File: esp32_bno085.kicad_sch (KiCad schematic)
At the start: 36 parts, among them J1 530480210, J2 USB_C_Receptacle_USB2.0_16P, Q1 AO3401A, SW1 RESET, SW2 BOOT, U1 TP4056-42-ESOP8, U2 ESP32-S3-WROOM-1, U3 BNO085, U4 XC6220B331MR, Y1 32.7680kHz

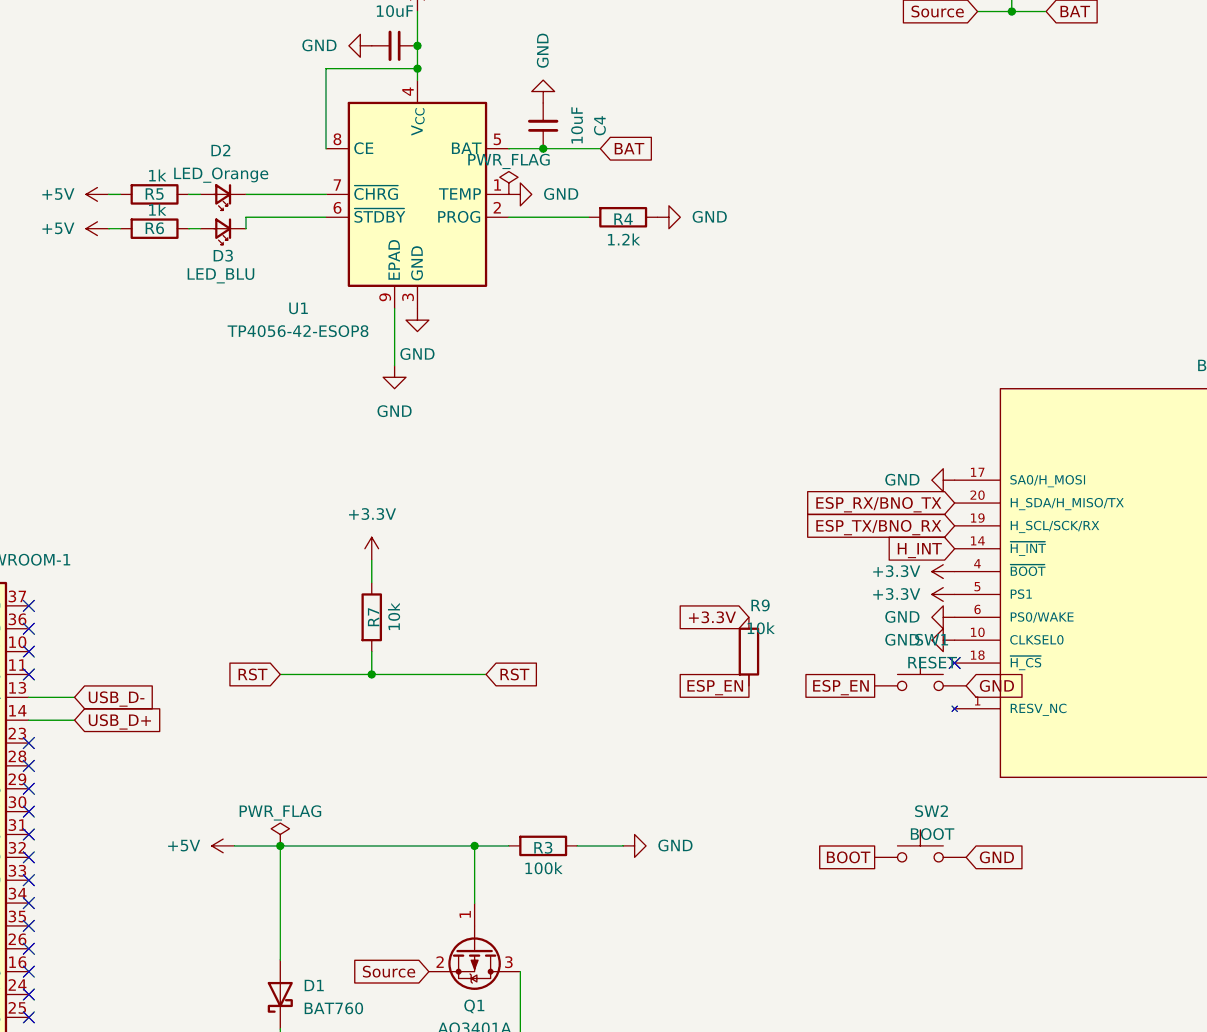
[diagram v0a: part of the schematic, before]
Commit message: Clean KiCad DRC warnings
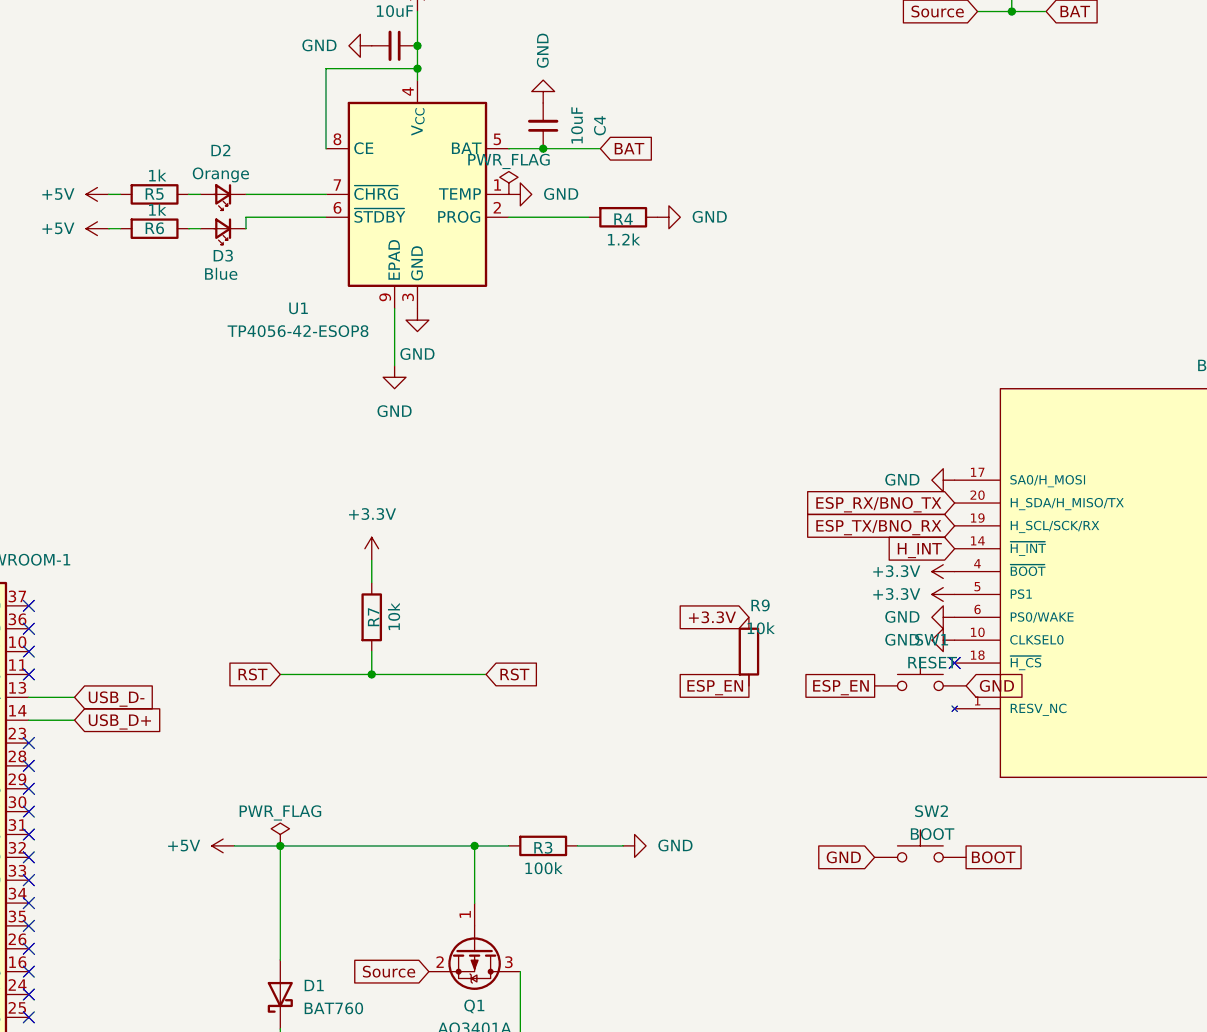
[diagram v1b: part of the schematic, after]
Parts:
- D2: value LED_Orange -> Orange
- D3: value LED_BLU -> Blue
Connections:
- net BOOT: now also SW2.2; no longer SW2.1
- net GND: now also SW2.1; no longer SW2.2
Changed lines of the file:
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@@
 			)
 		)
-		(property "Value" "LED_Orange"
+		(property "Value" "Orange"
 			(at 88.646 58.674 0)
 			(effects
@@
 			)
 		)
-		(property "Value" "LED_BLU"
+		(property "Value" "Blue"
 			(at 88.646 69.85 0)
 			(effects
@@
 		)
 	)
-	(global_label "BOOT"
-		(shape passive)
+	(global_label "GND"
+		(shape input)
 		(at 161.29 134.62 180)
 		(fields_autoplaced yes)
@@
 		)
 	)
-	(global_label "GND"
-		(shape input)
+	(global_label "BOOT"
+		(shape passive)
 		(at 171.45 134.62 0)
 		(fields_autoplaced yes)
